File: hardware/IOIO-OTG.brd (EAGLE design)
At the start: 68.6 x 30.5 mm, 60 parts, among them Q1 IRLML2244, Q2 2N7002PW, Q3 AO3404A, U1 PIC24FJ256GB206, U14 SWITCH_SPDT, U2 TPS62133RGTT, U3 VREG_MIC5216

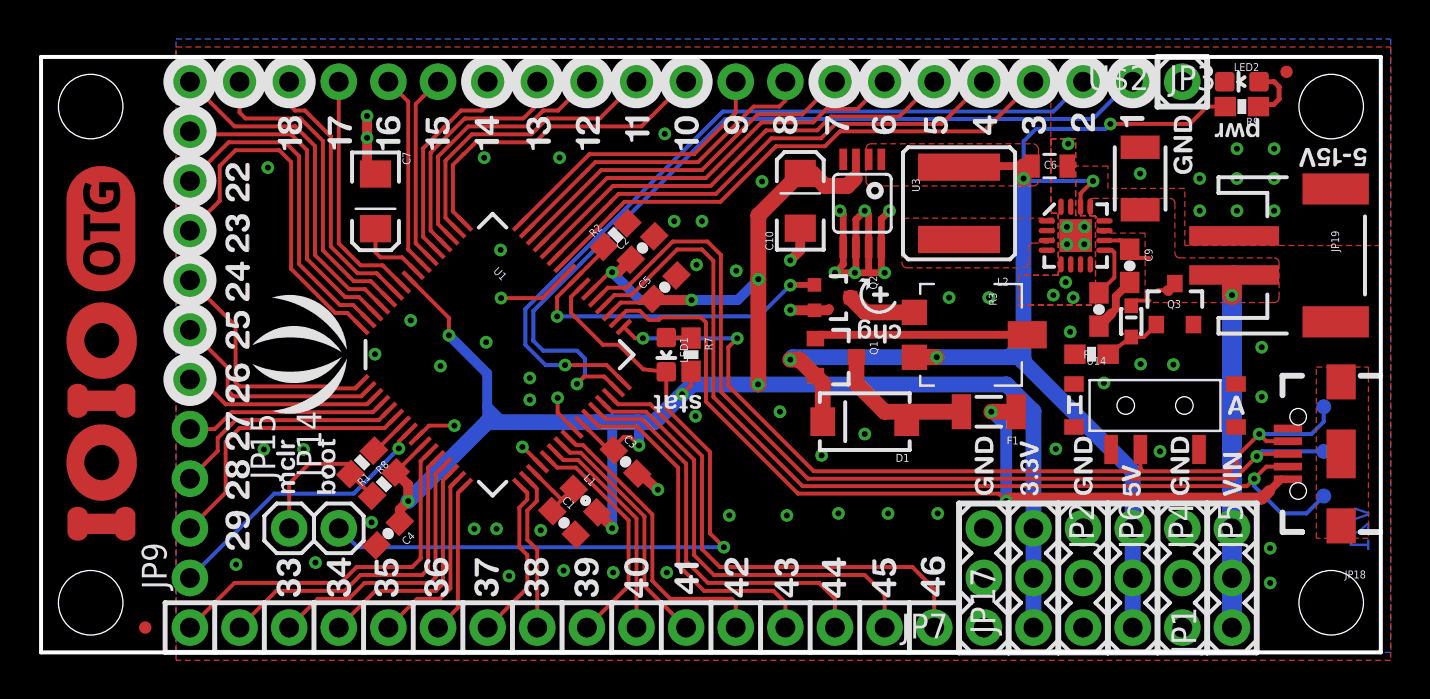
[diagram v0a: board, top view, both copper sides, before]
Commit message: Moved to v22 in sch/copper, updated frame in SCH
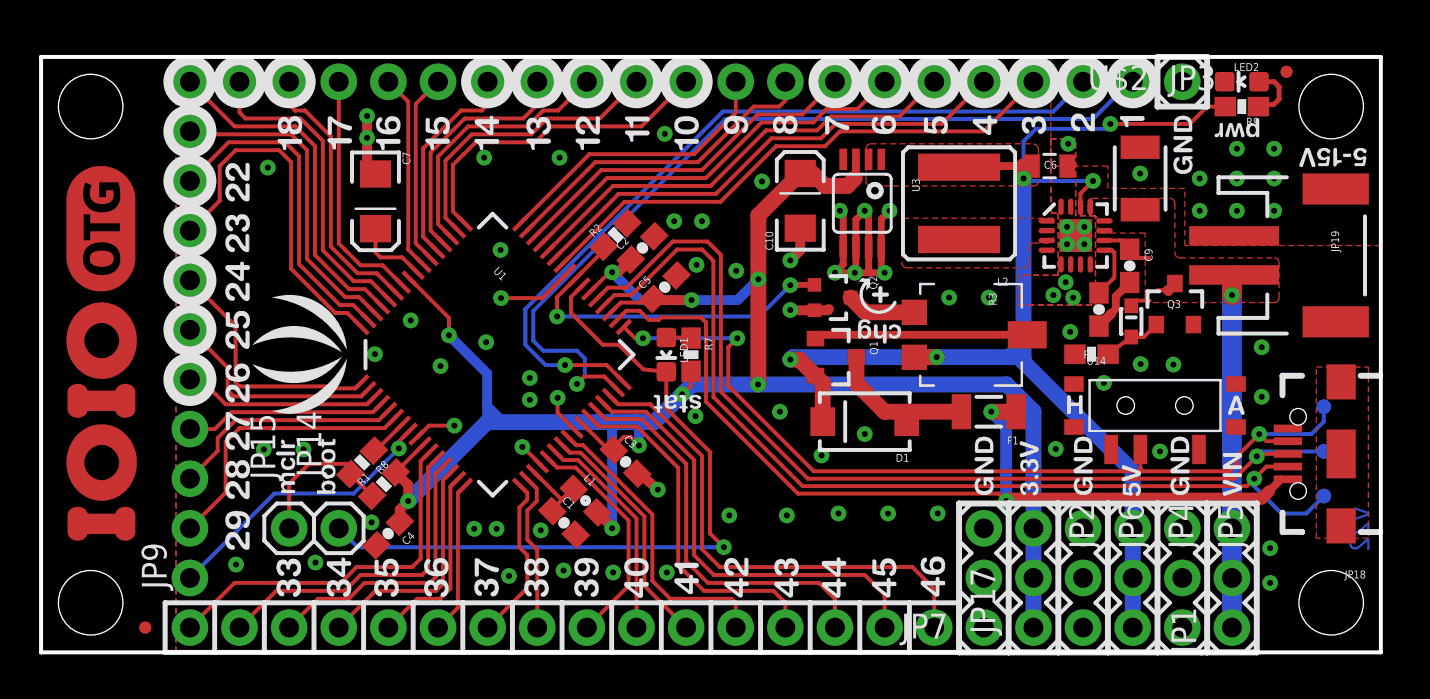
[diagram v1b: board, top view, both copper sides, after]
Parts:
- removed U$1: CREATIVE_COMMONS, SparkFun-Aesthetics:CREATIVE_COMMONS
- added FRAME2: FRAME-LEDGER, SparkFun-Aesthetics:CREATIVE_COMMONS
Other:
- board text added: "Aaron Weiss, Pete Lewis"
- board text added: "Revised by:"
- board text added: "Ytai Ben-tsvi"
- board text added: "v22"
- board text removed: "v21"
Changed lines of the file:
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@@
 <layer number="29" name="tStop" color="7" fill="3" visible="no" active="yes"/>
 <layer number="30" name="bStop" color="3" fill="6" visible="no" active="yes"/>
-<layer number="31" name="tCream" color="7" fill="4" visible="yes" active="yes"/>
+<layer number="31" name="tCream" color="7" fill="4" visible="no" active="yes"/>
 <layer number="32" name="bCream" color="3" fill="5" visible="no" active="yes"/>
 <layer number="33" name="tFinish" color="6" fill="3" visible="no" active="yes"/>
@@
 <circle x="55.88" y="29.21" radius="1.1039" width="0.508" layer="22"/>
 <circle x="53.34" y="29.21" radius="1.1039" width="0.508" layer="22"/>
-<text x="67.9958" y="7.4676" size="1.016" layer="16" font="vector" ratio="20" rot="SMR270">v21</text>
+<text x="67.9958" y="7.4676" size="1.016" layer="16" font="vector" ratio="20" rot="SMR270">v22</text>
 <wire x1="57.15" y1="30.48" x2="59.69" y2="30.48" width="0.3048" layer="21"/>
 <wire x1="59.69" y1="27.94" x2="59.69" y2="30.48" width="0.3048" layer="21"/>
@@
 <dimension x1="0" y1="30.48" x2="0" y2="0" x3="-4.572" y3="15.24" textsize="0.889" textratio="11" layer="47" unit="inch"/>
 <dimension x1="0" y1="30.48" x2="68.58" y2="30.48" x3="34.29" y3="35.433" textsize="0.889" textratio="11" layer="47" unit="inch"/>
+<text x="35.56" y="-11.43" size="1.778" layer="51" font="vector">Ytai Ben-tsvi</text>
+<text x="16.51" y="-14.224" size="1.778" layer="51" font="vector">Revised by:</text>
+<text x="34.29" y="-14.224" size="1.778" layer="51" font="vector">Aaron Weiss, Pete Lewis</text>
 </plain>
 <attributes>
@@
 </class>
 </classes>
-<designrules name="OSHPark *">
-<description language="de">&lt;b&gt;EAGLE Design Rules&lt;/b&gt;
+<designrules name="SparkFun-2-layer *">
+<description language="en">&lt;b&gt;EAGLE Design Rules&lt;/b&gt;
 &lt;p&gt;
-Die Standard-Design-Rules sind so gewählt, dass sie für
-die meisten Anwendungen passen. Sollte ihre Platine
-besondere Anforderungen haben, treffen Sie die erforderlichen
-Einstellungen hier und speichern die Design Rules unter
-einem neuen Namen ab.</description>
-<description language="en">&lt;b&gt;Laen's PCB Order Design Rules&lt;/b&gt;
-&lt;p&gt;
-Please make sure your boards conform to these design rules.</description>
+The default Design Rules have been set to cover
+a wide range of applications. Your particular design
+may have different requirements, so please make the
+necessary adjustments and save your customized
+design rules under a new name.</description>
 <param name="layerSetup" value="(1*16)"/>
-<param name="mtCopper" value="0.0356mm 0.0356mm 0.0356mm 0.0356mm 0.0356mm 0.0356mm 0.0356mm 0.0356mm 0.0356mm 0.0356mm 0.0356mm 0.0356mm 0.0356mm 0.0356mm 0.0356mm 0.0356mm"/>
-<param name="mtIsolate" value="1.5011mm 0.1499mm 0.2007mm 0.1499mm 0.2007mm 0.1499mm 0.2007mm 0.1499mm 0.2007mm 0.1499mm 0.2007mm 0.1499mm 0.2007mm 0.1499mm 0.2007mm"/>
+<param name="mtCopper" value="0.035mm 0.035mm 0.035mm 0.035mm 0.035mm 0.035mm 0.035mm 0.035mm 0.035mm 0.035mm 0.035mm 0.035mm 0.035mm 0.035mm 0.035mm 0.035mm"/>
+<param name="mtIsolate" value="1.5mm 0.15mm 0.2mm 0.15mm 0.2mm 0.15mm 0.2mm 0.15mm 0.2mm 0.15mm 0.2mm 0.15mm 0.2mm 0.15mm 0.2mm"/>
 <param name="mdWireWire" value="6mil"/>
 <param name="mdWirePad" value="6mil"/>
@@
 <param name="mdViaViaSameLayer" value="8mil"/>
 <param name="mnLayersViaInSmd" value="2"/>
-<param name="mdCopperDimension" value="15mil"/>
-<param name="mdDrill" value="6mil"/>
+<param name="mdCopperDimension" value="8mil"/>
+<param name="mdDrill" value="8mil"/>
 <param name="mdSmdStop" value="0mil"/>
-<param name="msWidth" value="6mil"/>
-<param name="msDrill" value="10mil"/>
-<param name="msMicroVia" value="10mil"/>
+<param name="msWidth" value="7mil"/>
+<param name="msDrill" value="12mil"/>
+<param name="msMicroVia" value="9.99mm"/>
 <param name="msBlindViaRatio" value="0.5"/>
 <param name="rvPadTop" value="0.25"/>
@@
 <param name="rvMicroViaOuter" value="0.25"/>
 <param name="rvMicroViaInner" value="0.25"/>
-<param name="rlMinPadTop" value="7mil"/>
+<param name="rlMinPadTop" value="12mil"/>
 <param name="rlMaxPadTop" value="20mil"/>
-<param name="rlMinPadInner" value="7mil"/>
+<param name="rlMinPadInner" value="10mil"/>
 <param name="rlMaxPadInner" value="20mil"/>
-<param name="rlMinPadBottom" value="7mil"/>
+<param name="rlMinPadBottom" value="12mil"/>
 <param name="rlMaxPadBottom" value="20mil"/>
-<param name="rlMinViaOuter" value="7mil"/>
+<param name="rlMinViaOuter" value="10mil"/>
 <param name="rlMaxViaOuter" value="20mil"/>
-<param name="rlMinViaInner" value="7mil"/>
+<param name="rlMinViaInner" value="10mil"/>
 <param name="rlMaxViaInner" value="20mil"/>
 <param name="rlMinMicroViaOuter" value="4mil"/>
@@
 <param name="mvStopFrame" value="1"/>
 <param name="mvCreamFrame" value="0"/>
-<param name="mlMinStopFrame" value="3mil"/>
-<param name="mlMaxStopFrame" value="3mil"/>
+<param name="mlMinStopFrame" value="4mil"/>
+<param name="mlMaxStopFrame" value="4mil"/>
 <param name="mlMinCreamFrame" value="0mil"/>
 <param name="mlMaxCreamFrame" value="0mil"/>
-<param name="mlViaStopLimit" value="12mil"/>
+<param name="mlViaStopLimit" value="20mil"/>
 <param name="srRoundness" value="0"/>
 <param name="srMinRoundness" value="0mil"/>
@@
 <attribute name="VALUE" x="13.97" y="3.175" size="1.27" layer="27"/>
 </element>
-<element name="U$1" library="SparkFun-Aesthetics" package="CREATIVE_COMMONS" value="CREATIVE_COMMONS" x="4.318" y="-9.7536" smashed="yes"/>
 <element name="JP8" library="SparkFun" package="MICRO-FIDUCIAL" value="FIDUCIALUFIDUCIAL" x="5.334" y="1.27" smashed="yes"/>
 <element name="JP16" library="SparkFun" package="MICRO-FIDUCIAL" value="FIDUCIALUFIDUCIAL" x="63.754" y="29.718" smashed="yes"/>
@@
 </element>
 <element name="LOGO1" library="SparkFun-Aesthetics" package="OSHW-LOGO-S" value="OSHW-LOGOS" x="66.421" y="15.24" rot="MR270"/>
+<element name="FRAME2" library="SparkFun-Aesthetics" package="CREATIVE_COMMONS" value="FRAME-LEDGER" x="5.08" y="-11.43"/>
 </elements>
 <signals>
@@
 <via x="33.8328" y="22.0726" extent="1-16" drill="0.3048" diameter="0.635"/>
 <polygon width="0.2032" layer="1" isolate="0.3048" thermals="no" rank="6">
-<vertex x="6.9088" y="30.988"/>
-<vertex x="69.088" y="30.988"/>
-<vertex x="69.088" y="-0.4064"/>
-<vertex x="6.9088" y="-0.4064"/>
+<vertex x="6.9088" y="30.48"/>
+<vertex x="68.58" y="30.48"/>
+<vertex x="68.58" y="0"/>
+<vertex x="6.9088" y="0"/>
 </polygon>
 <polygon width="0.2032" layer="16" isolate="0.3048" thermals="no" rank="6">
-<vertex x="6.9088" y="31.3944"/>
-<vertex x="69.088" y="31.3944"/>
-<vertex x="69.088" y="0"/>
+<vertex x="6.9088" y="30.48"/>
+<vertex x="68.58" y="30.48"/>
+<vertex x="68.58" y="0"/>
 <vertex x="6.9088" y="0"/>
 </polygon>
@@
 <wire x1="55.8038" y1="17.7418" x2="56.0706" y2="18.0086" width="0.2032" layer="1"/>
 <wire x1="56.0706" y1="18.0086" x2="56.7436" y2="18.0086" width="0.2032" layer="1"/>
-<wire x1="55.753" y1="20.193" x2="55.7276" y2="20.6366" width="0" layer="19" extent="1-1"/>
+<wire x1="55.753" y1="20.193" x2="55.753" y2="20.6112" width="0.254" layer="1"/>
+<wire x1="55.753" y1="20.6112" x2="55.7276" y2="20.6366" width="0.254" layer="1"/>
 </signal>
 <signal name="N$4">

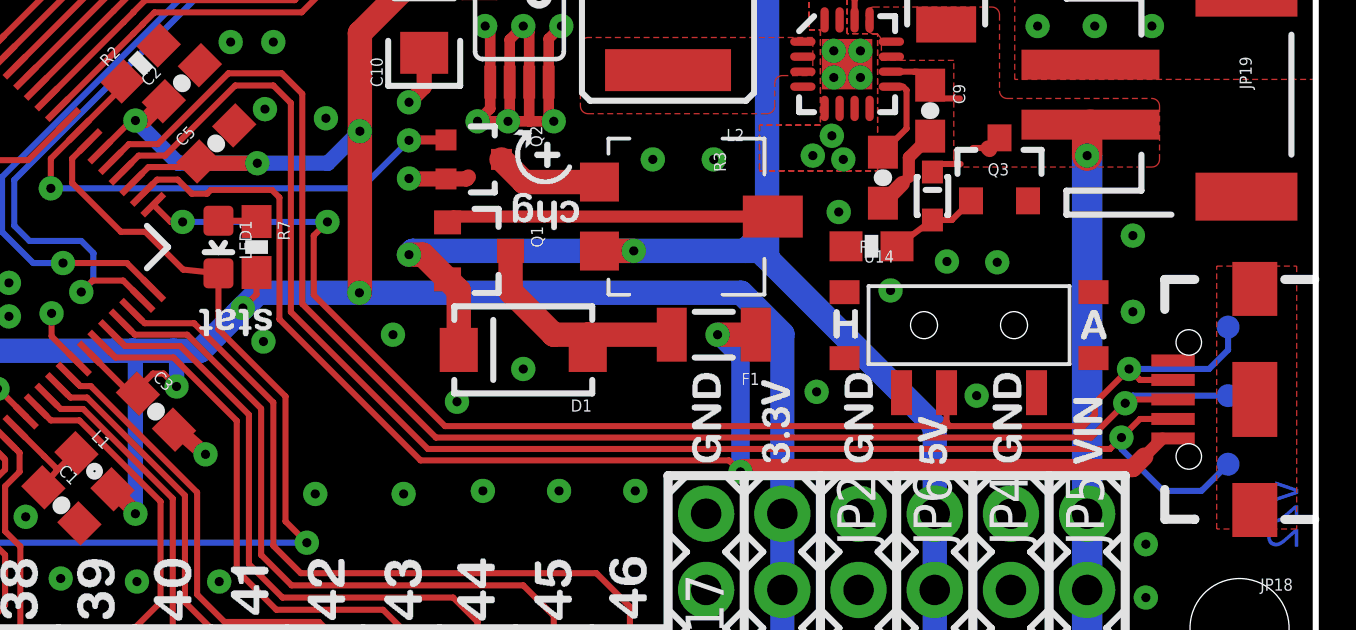
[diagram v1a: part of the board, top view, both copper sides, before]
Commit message: Restored back to 1.6K and 750 ohm LED resistors
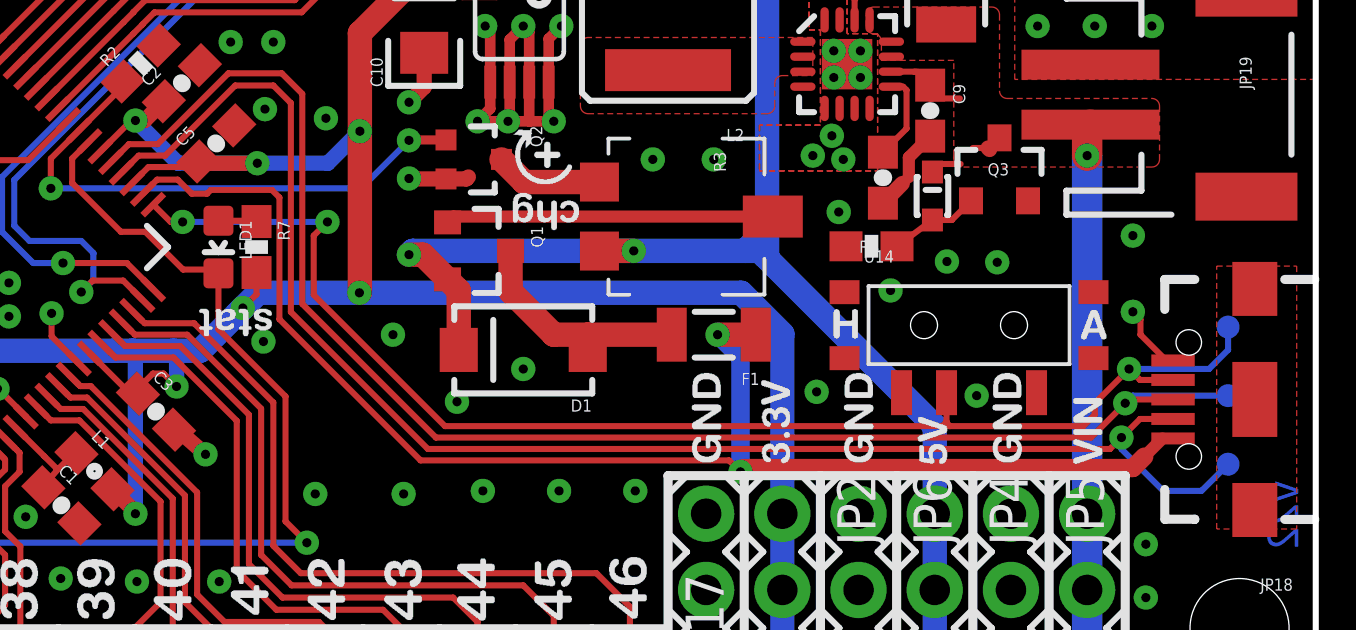
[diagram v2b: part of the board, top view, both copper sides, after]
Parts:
- LED2: value RED -> Red
- R7: value 330 -> 750
- R9: value 330 -> 1.6K
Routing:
- net GND: track 37.4 -> 39.7 mm
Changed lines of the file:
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@@
 <setting verticaltext="up"/>
 </settings>
-<grid distance="0.05" unitdist="inch" unit="inch" style="lines" multiple="2" display="yes" altdistance="0.001" altunitdist="inch" altunit="inch"/>
+<grid distance="0.05" unitdist="inch" unit="inch" style="lines" multiple="2" display="yes" altdistance="0.005" altunitdist="inch" altunit="inch"/>
 <layers>
 <layer number="1" name="Top" color="4" fill="1" visible="yes" active="yes"/>
@@
 <layer number="47" name="Measures" color="7" fill="1" visible="no" active="yes"/>
 <layer number="48" name="Document" color="7" fill="1" visible="no" active="yes"/>
-<layer number="49" name="Reference" color="7" fill="1" visible="yes" active="yes"/>
+<layer number="49" name="Reference" color="7" fill="1" visible="no" active="yes"/>
 <layer number="50" name="dxf" color="7" fill="1" visible="no" active="yes"/>
 <layer number="51" name="tDocu" color="6" fill="1" visible="yes" active="yes"/>
@@
 <attribute name="VALUE" x="52.705" y="7.62" size="1.27" layer="27" rot="R270"/>
 </element>
-<element name="R7" library="SparkFun-Resistors" package="0603-RES" value="330" x="33.274" y="15.24" smashed="yes" rot="R270">
+<element name="R7" library="SparkFun-Resistors" package="0603-RES" value="750" x="33.274" y="15.24" smashed="yes" rot="R270">
 <attribute name="NAME" x="33.9725" y="16.129003125" size="0.4064" layer="25" rot="R270"/>
-<attribute name="VALUE" value="330" x="32.131" y="16.319503125" size="0.4064" layer="27" rot="R270"/>
-<attribute name="PROD_ID" value="RES-00818" x="33.274" y="15.24" size="1.778" layer="27" rot="R270" display="off"/>
+<attribute name="VALUE" value="750" x="32.131" y="16.319503125" size="0.4064" layer="27" rot="R270"/>
+<attribute name="PROD_ID" value="RES-07824" x="33.274" y="15.24" size="1.778" layer="27" rot="R270" display="off"/>
 </element>
 <element name="R8" library="SparkFun-Resistors" package="0603-RES" value="470" x="16.4338" y="9.7282" smashed="yes" rot="R225">
@@
 <element name="LED1" library="SparkFun-LED" package="LED-0603" value="Yellow" x="32.004" y="15.24" smashed="yes" rot="R180">
 <attribute name="NAME" x="32.7025" y="16.129" size="0.4064" layer="25" rot="R270"/>
-<attribute name="PROD_ID" value="DIO-09003" x="32.004" y="15.24" size="1.778" layer="27" rot="R180" display="off"/>
+<attribute name="PROD_ID" value="DIO-11230" x="32.004" y="15.24" size="1.778" layer="27" rot="R180" display="off"/>
 <attribute name="VALUE" value="Yellow" x="32.004" y="15.24" size="1.778" layer="27" rot="R180" display="off"/>
 </element>
@@
 <attribute name="VALUE" x="55.245" y="7.62" size="1.27" layer="27" rot="R270"/>
 </element>
-<element name="R9" library="SparkFun-Resistors" package="0603-RES" value="330" x="61.468" y="27.94" smashed="yes" rot="R180">
+<element name="R9" library="SparkFun-Resistors" package="0603-RES" value="1.6K" x="61.468" y="27.94" smashed="yes" rot="R180">
 <attribute name="NAME" x="62.357" y="27.3685" size="0.4064" layer="25" rot="R180"/>
-<attribute name="VALUE" value="330" x="62.5475" y="29.083" size="0.4064" layer="27" rot="R180"/>
-<attribute name="PROD_ID" value="RES-00818" x="61.468" y="27.94" size="1.778" layer="27" rot="R180" display="off"/>
+<attribute name="VALUE" value="1.6K" x="62.5475" y="29.083" size="0.4064" layer="27" rot="R180"/>
+<attribute name="PROD_ID" value="RES-08361" x="61.468" y="27.94" size="1.778" layer="27" rot="R180" display="off"/>
 </element>
-<element name="LED2" library="SparkFun-LED" package="LED-0603" value="RED" x="61.468" y="29.21" smashed="yes" rot="R90">
+<element name="LED2" library="SparkFun-LED" package="LED-0603" value="Red" x="61.468" y="29.21" smashed="yes" rot="R90">
 <attribute name="NAME" x="62.357" y="30.1625" size="0.4064" layer="25" rot="R180"/>
-<attribute name="PROD_ID" value="DIO-00819" x="61.468" y="29.21" size="1.778" layer="27" rot="R90" display="off"/>
-<attribute name="VALUE" value="RED" x="61.468" y="29.21" size="1.778" layer="27" rot="R90" display="off"/>
+<attribute name="PROD_ID" value="DIO-11154" x="61.468" y="29.21" size="1.778" layer="27" rot="R90" display="off"/>
+<attribute name="VALUE" value="Red" x="61.468" y="29.21" size="1.778" layer="27" rot="R90" display="off"/>
 </element>
 <element name="JP15" library="SparkFun" package="1X01" value="M01PTH" x="12.7" y="6.35" smashed="yes">
@@
 <wire x1="55.0164" y1="17.5768" x2="55.0164" y2="18.2254" width="0.4064" layer="1"/>
 <wire x1="55.0164" y1="18.2254" x2="55.7276" y2="18.9366" width="0.4064" layer="1"/>
+<wire x1="63.823" y1="11.46" x2="63.597" y2="11.46" width="0.2032" layer="1"/>
+<wire x1="63.597" y1="11.46" x2="62.738" y2="12.319" width="0.2032" layer="1"/>
+<wire x1="62.738" y1="12.319" x2="62.738" y2="12.827" width="0.2032" layer="1"/>
+<wire x1="62.738" y1="12.827" x2="62.484" y2="13.081" width="0.2032" layer="1"/>
 </signal>
 <signal name="P7">
@@
 <wire x1="27.1272" y1="17.3736" x2="28.7528" y2="15.748" width="0.2032" layer="1"/>
 <wire x1="28.7528" y1="15.748" x2="29.5656" y2="15.748" width="0.2032" layer="1"/>
-<wire x1="32.004" y1="14.363" x2="30.8236" y2="14.49" width="0.2032" layer="1"/>
 <wire x1="30.8236" y1="14.49" x2="29.5656" y2="15.748" width="0.2032" layer="1"/>
 <wire x1="32.004" y1="14.363" x2="32.004" y2="12.4968" width="0.2032" layer="1"/>
@@
 <wire x1="34.9504" y1="5.3848" x2="16.2052" y2="5.3848" width="0.2032" layer="16"/>
 <wire x1="16.2052" y1="5.3848" x2="15.24" y2="6.35" width="0.2032" layer="16"/>
+<wire x1="30.8236" y1="14.49" x2="31.877" y2="14.49" width="0.2032" layer="1"/>
+<wire x1="31.877" y1="14.49" x2="32.004" y2="14.363" width="0.2032" layer="1"/>
 </signal>
 <signal name="N$1">
